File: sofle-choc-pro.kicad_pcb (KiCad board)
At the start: 2 copper layers, 129 x 119 mm, 196 parts, among them J1 Connector, USB-TYPE-C-16P, J2 Connector, USB-TYPE-C-16P, J3 OLED 128x32 / nice!view, SW1 BOOT, SW10 F0, SW11 F1, SW12 F2, SW13 F3, SW14 F4, SW15 F5, SW16 F6 Choc/EC11, SW2 RESET, SW20 N0, SW21 N1, SW22 N2, SW23 N3, SW24 N4, SW25 N5, SW30 T0, SW31 T1, SW32 T2, SW33 T3, SW34 T4, SW35 T5, SW40 H0, SW41 H1, SW42 H2, SW43 H3, SW44 H4, SW45 H5, SW50 B0, SW51 B1, SW52 B2, SW53 B3, SW54 B4, SW55 B5, SW60 TH0, SW61 TH1, SW62 TH2, SW63 TH3, SW64 TH4, SW65 TH5 Choc/EC11, U1 RP2040, U2 SRV05-4, U3 W25Q128, U4 SRV05-4, U5 AP2112K-3.3, U6 SN74LV1T34DBVR, X1 ABM8-272-T3

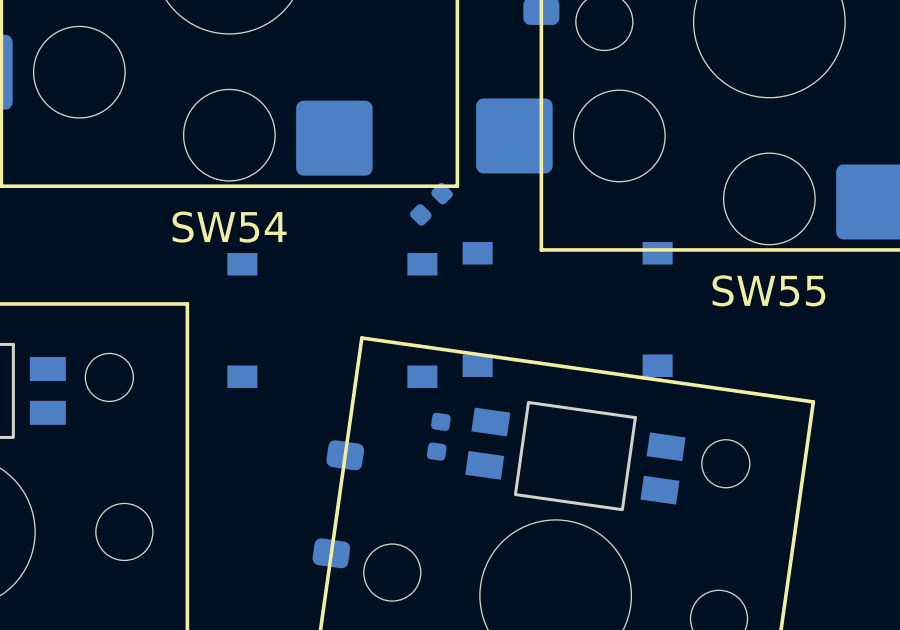
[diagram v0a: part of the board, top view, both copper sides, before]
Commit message: feat(pcb): use 2-pin ts-1088 buttons for boot and reset
BOOT and RESET (SW1, SW2) now use the smaller 2-terminal XUNPU
TS-1088-AR02016 tactile switch instead of the 4-pin TS-1187A.

- LCSC C720477 is a JLCPCB Basic part, so no extended-part fee
- 4 x 3 mm body with one pad per short end, easier to fit and route
- Footprint and STEP model live in the project library, so the board
  does not depend on the PCM JLCPCB library being installed

Swapped in place: same position, side, rotation and nets. ERC 0 errors;
DRC counts did not rise and schematic parity passes.
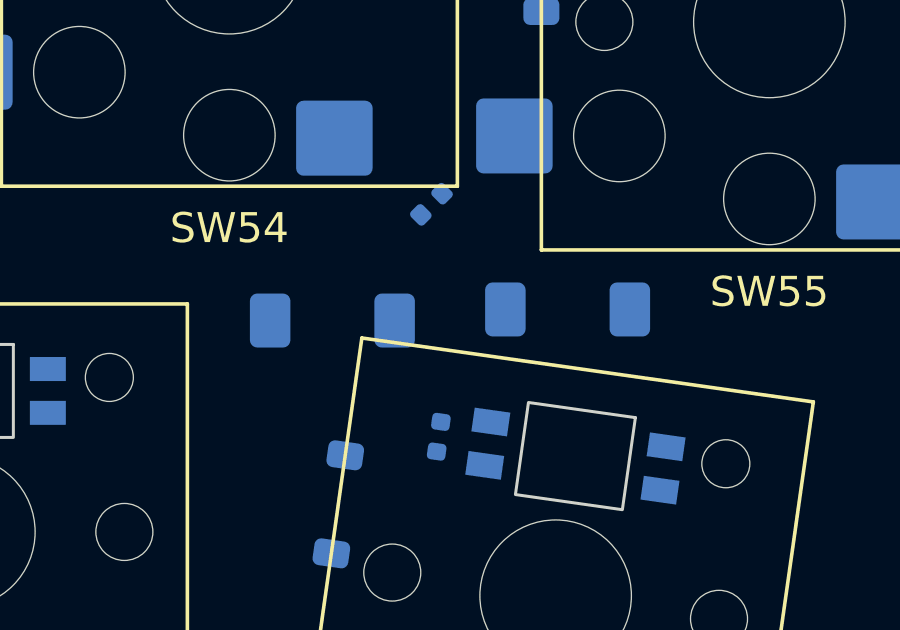
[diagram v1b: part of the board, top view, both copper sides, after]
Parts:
- SW1, SW2: footprint my-soffle:SW_Push_1P1T_XKB_TS-1187A -> my-soffle:SW_Push_1P1T_XUNPU_TS-1088-AR02016

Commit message: feat(sch): protect the link port and harden master detection
The link USB-C port could back-feed 5 V into a misplugged device and its
data line had no current limit, and diode leakage could fool the VBUS
divider on the secondary half. These fixes follow the reference boards
with a real USB-C link (Djinn, YAEMK) and Splinky's detect divider.

- F2 polyfuse (same part as F1) between J2 VBUS and +5V; the connector
  side is now LINK_VBUS, and J2 CC stays open so hosts keep VBUS off
- R16 120 ohm between J2/U2 and GP12 (net LINK_DATA on the connector
  side) limits ESD clamp current and damps cable ringing
- R10/R11 now 5.1k/10k (was 10k/15k): same 3.3 V at GP13 with a stiffer
  divider against D1 reverse leakage
- HOST and LINK labels on the back silkscreen next to J1 and J2

ERC 0 errors. DRC with schematic parity: only starved_thermal and the
expected unconnected items (board still unrouted).
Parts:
- added F2: 500mA, Fuse:Fuse_1206_3216Metric, B.Cu at (167.7, 96.0)
- added R16: 120Ω, PCM_JLCPCB:R_0402, B.Cu at (164.5, 88.6)
- R10: value 10kΩ -> 5.1kΩ
- R11: value 15kΩ -> 10kΩ
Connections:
- J2 pad A6: GP12 -> LINK_DATA
- J2 pad A9B4: +5V -> LINK_VBUS
- J2 pad B6: GP12 -> LINK_DATA
- J2 pad B9A4: +5V -> LINK_VBUS
- U2 pad 1: GP12 -> LINK_DATA
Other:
- board text added: "HOST"
- board text added: "LINK"

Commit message: feat(sch): move the matrix onto the rp2040 side facing the keys
All six rows sat on GP0-GP6, on the far side of the RP2040 from the key
block, so every row wire had to cross the package before reaching the
matrix. The matrix now uses pins 29-41, which face the keys, in the
order the bundle peels off.

- Rows 1-6 (top to thumbs) on GP29-GP24, columns 0-5 (outer to inner)
  on GP18-GP23; the encoder-key column stays on GP5
- Second encoder moves to GP3/GP4, handedness JP1 to GP2, and the
  display I2C option to GP16 (SDA) / GP17 (SCL), still I2C0
- GP0, GP1, GP6 and GP9 are now unused with no-connect flags
- Board pads re-netted from the new netlist (87 pads)

QMK pin lists must follow this map. ERC 0 errors; DRC with schematic
parity shows only the expected unconnected items and starved thermals.
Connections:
- D10 pad 1: GP6 -> GP29
- D11 pad 1: GP6 -> GP29
- D12 pad 1: GP6 -> GP29
- D13 pad 1: GP6 -> GP29
- D14 pad 1: GP6 -> GP29
- D15 pad 1: GP6 -> GP29
- D16 pad 1: GP6 -> GP29
- D20 pad 1: GP0 -> GP28
- D21 pad 1: GP0 -> GP28
- D22 pad 1: GP0 -> GP28
- D23 pad 1: GP0 -> GP28
- D24 pad 1: GP0 -> GP28
- D25 pad 1: GP0 -> GP28
- D30 pad 1: GP1 -> GP27
- D31 pad 1: GP1 -> GP27
- D32 pad 1: GP1 -> GP27
- D33 pad 1: GP1 -> GP27
- D34 pad 1: GP1 -> GP27
- D35 pad 1: GP1 -> GP27
- D40 pad 1: GP2 -> GP26
- D41 pad 1: GP2 -> GP26
- D42 pad 1: GP2 -> GP26
- D43 pad 1: GP2 -> GP26
- D44 pad 1: GP2 -> GP26
- D45 pad 1: GP2 -> GP26
- D50 pad 1: GP3 -> GP25
- D51 pad 1: GP3 -> GP25
- D52 pad 1: GP3 -> GP25
- D53 pad 1: GP3 -> GP25
- D54 pad 1: GP3 -> GP25
- D55 pad 1: GP3 -> GP25
- D60 pad 1: GP4 -> GP24
- D61 pad 1: GP4 -> GP24
- D62 pad 1: GP4 -> GP24
- D63 pad 1: GP4 -> GP24
- D64 pad 1: GP4 -> GP24
- D65 pad 1: GP4 -> GP24
- JP1 pad 2: GP21 -> GP2
- JP2 pad 1: GP29 -> GP17
- JP3 pad 1: GP28 -> GP16
- R12 pad 2: GP28 -> GP16
- R13 pad 2: GP29 -> GP17
- SW10 pad 1: GP27 -> GP18
- SW11 pad 1: GP26 -> GP19
- SW12 pad 1: GP25 -> GP20
- SW13 pad 1: GP24 -> GP21
- SW14 pad 1: GP19 -> GP22
- SW15 pad 1: GP18 -> GP23
- SW20 pad 1: GP27 -> GP18
- SW21 pad 1: GP26 -> GP19
- SW22 pad 1: GP25 -> GP20
- SW23 pad 1: GP24 -> GP21
- SW24 pad 1: GP19 -> GP22
- SW25 pad 1: GP18 -> GP23
- SW30 pad 1: GP27 -> GP18
- SW31 pad 1: GP26 -> GP19
- SW32 pad 1: GP25 -> GP20
- SW33 pad 1: GP24 -> GP21
- SW34 pad 1: GP19 -> GP22
- SW35 pad 1: GP18 -> GP23
- SW40 pad 1: GP27 -> GP18
- SW41 pad 1: GP26 -> GP19
- SW42 pad 1: GP25 -> GP20
- SW43 pad 1: GP24 -> GP21
- SW44 pad 1: GP19 -> GP22
- SW45 pad 1: GP18 -> GP23
- SW50 pad 1: GP27 -> GP18
- SW51 pad 1: GP26 -> GP19
- SW52 pad 1: GP25 -> GP20
- SW53 pad 1: GP24 -> GP21
- SW54 pad 1: GP19 -> GP22
- SW55 pad 1: GP18 -> GP23
- SW60 pad 1: GP27 -> GP18
- SW61 pad 1: GP26 -> GP19
- SW62 pad 1: GP25 -> GP20
- SW63 pad 1: GP24 -> GP21
- SW64 pad 1: GP19 -> GP22
- SW65 pad 1: GP18 -> GP23
- SW65 pad A: GP23 -> GP4
- SW65 pad B: GP22 -> GP3
- U1 pad 2: GP0 -> unconnected-(U1-GPIO0-Pad2)
- U1 pad 27: unconnected-(U1-GPIO16-Pad27) -> GP16
- U1 pad 28: unconnected-(U1-GPIO17-Pad28) -> GP17
- U1 pad 3: GP1 -> unconnected-(U1-GPIO1-Pad3)
- U1 pad 31: unconnected-(U1-GPIO20-Pad31) -> GP20
- U1 pad 8: GP6 -> unconnected-(U1-GPIO6-Pad8)
